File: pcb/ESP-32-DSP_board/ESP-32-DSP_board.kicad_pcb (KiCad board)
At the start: 2 copper layers, 40.4 x 74.6 mm, 56 parts, among them J1 USB_C_Receptacle_USB2.0, J2 Conn_01x04_Pin, J3 Conn_01x04_Pin, J4 Conn_01x07_Pin, J5 Conn_01x07_Pin, Q1 BC847, Q2 BC847, SW1 Reset, SW2 Boot, U1 AZ1117IH-3.3, U2 ESP32-WROOM-32UE-N8, U3 USBLC6-2P6, U4 CP2104, U5 ADS8688

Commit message: Separated GND and GNDA
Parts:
- added NT1: NetTie_2, NetTie:NetTie-2_THT_Pad1.0mm, F.Cu at (104.1, 86.6)
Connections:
- C19 pad 2: Net-(U5-AIN_0GND) -> GNDA
- C20 pad 2: Net-(U5-AIN_1GND) -> GNDA
- C21 pad 1: Net-(U5-AIN_2GND) -> GNDA
- C22 pad 1: Net-(U5-AIN_3GND) -> GNDA
- C23 pad 1: Net-(U5-AIN_4GND) -> GNDA
- C24 pad 1: Net-(U5-AIN_5GND) -> GNDA
- C25 pad 2: Net-(U5-AIN_6GND) -> GNDA
- C26 pad 1: Net-(U5-AIN_7GND) -> GNDA
- U5 pad 10: GND -> GNDA
- U5 pad 11: GND -> GNDA
- U5 pad 13: Net-(U5-AIN_6GND) -> GNDA
- U5 pad 15: Net-(U5-AIN_7GND) -> GNDA
- U5 pad 17: Net-(U5-AIN_0GND) -> GNDA
- U5 pad 19: Net-(U5-AIN_1GND) -> GNDA
- U5 pad 20: Net-(U5-AIN_2GND) -> GNDA
- U5 pad 22: Net-(U5-AIN_3GND) -> GNDA
- U5 pad 24: Net-(U5-AIN_4GND) -> GNDA
- U5 pad 26: Net-(U5-AIN_5GND) -> GNDA
- U5 pad 28: GND -> GNDA
- U5 pad 29: GND -> GNDA
- U5 pad 31: GND -> GNDA
- U5 pad 32: GND -> GNDA
- U5 pad 8: GND -> GNDA
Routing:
- net GNDA: track 0.00 -> 95.9 mm, vias 0 -> 12
- net Net-(U5-AIN_6GND): track 8.24 -> 0.00 mm
- net Net-(U5-AIN_1GND): track 8.12 -> 0.00 mm
- net Net-(U5-AIN_7GND): track 7.86 -> 0.00 mm
- net Net-(U5-AIN_0GND): track 7.62 -> 0.00 mm
- net Net-(U5-AIN_2GND): track 7.22 -> 0.00 mm
- net Net-(U5-AIN_3GND): track 7.15 -> 0.00 mm
- net Net-(U5-AIN_4GND): track 6.78 -> 0.00 mm
- net Net-(U5-AIN_5GND): track 6.65 -> 0.00 mm
- net GND: track 160.5 -> 154.1 mm, vias 42 -> 37
- net /ADC_A5: vias 0 -> 1
- net /ADC_A4: vias 0 -> 1
- net /ADC_A3: vias 0 -> 1
- net /ADC_A2: vias 0 -> 1
- added copper zone on B.Cu, net GNDA
- added copper zone on F.Cu, net GNDA

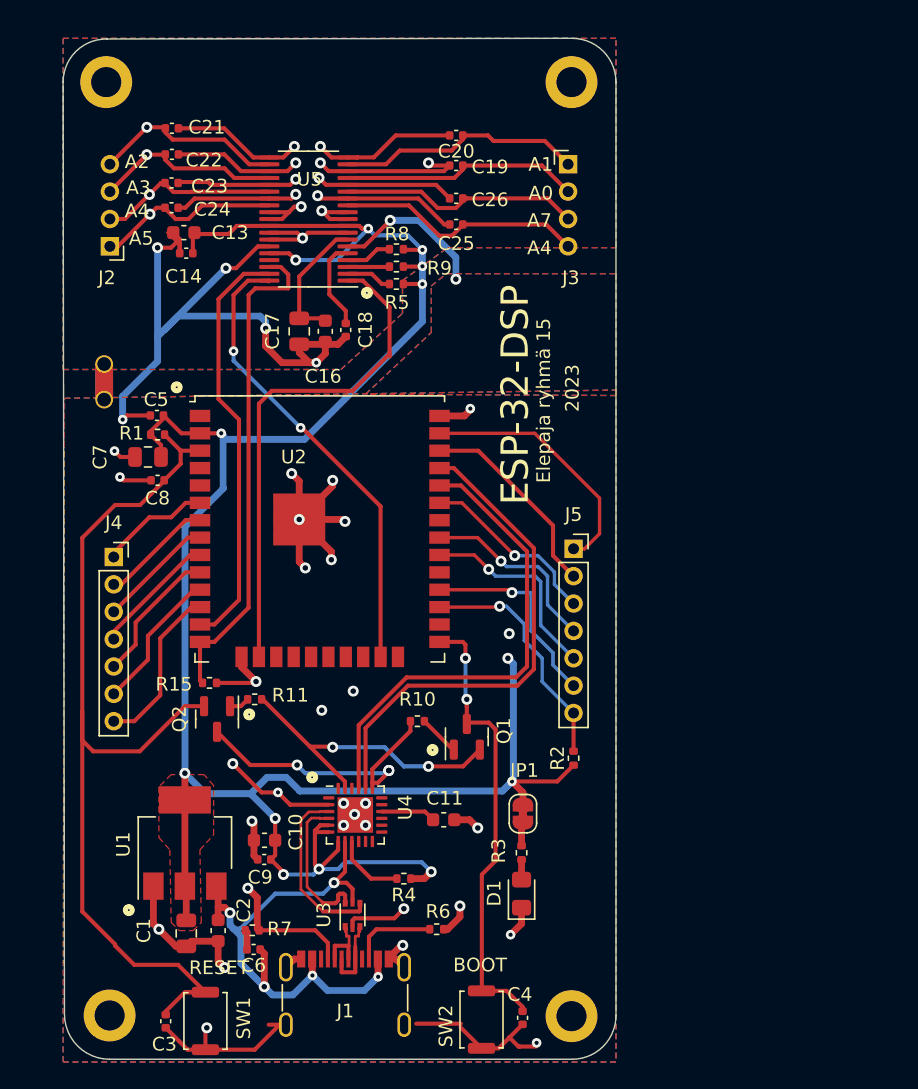
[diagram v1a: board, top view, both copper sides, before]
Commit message: Updated ADC configutation
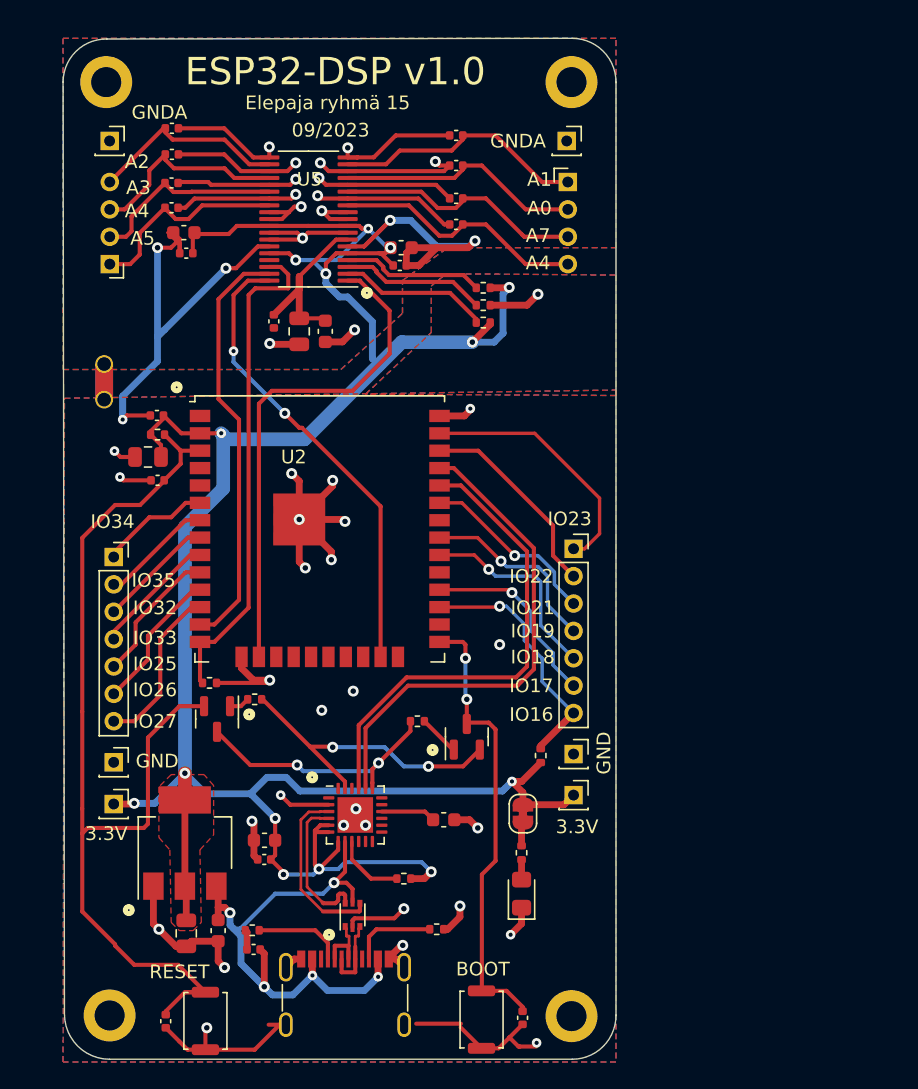
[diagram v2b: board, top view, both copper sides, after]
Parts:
- added C12: 100n, Capacitor_SMD:C_0402_1005Metric, F.Cu at (116.5, 83.5)
- added C15: 100n, Capacitor_SMD:C_0402_1005Metric, F.Cu at (125.7, 79.4)
- added J10: Conn_01x01_Pin, Connector_PinSocket_2.00mm:PinSocket_1x01_P2.00mm_Vertical, F.Cu at (104.5, 70.3)
- added J11: Conn_01x01_Pin, Connector_PinSocket_2.00mm:PinSocket_1x01_P2.00mm_Vertical, F.Cu at (137.9, 70.3)
- added J6: Conn_01x01_Pin, Connector_PinSocket_2.00mm:PinSocket_1x01_P2.00mm_Vertical, F.Cu at (104.8, 115.7)
- added J7: Conn_01x01_Pin, Connector_PinSocket_2.00mm:PinSocket_1x01_P2.00mm_Vertical, F.Cu at (138.4, 115.1)
- added J8: Conn_01x01_Pin, Connector_PinSocket_2.00mm:PinSocket_1x01_P2.00mm_Vertical, F.Cu at (104.8, 118.8)
- added J9: Conn_01x01_Pin, Connector_PinSocket_2.00mm:PinSocket_1x01_P2.00mm_Vertical, F.Cu at (138.4, 118.1)
- C18: value 100n -> 1u; footprint Capacitor_SMD:C_0402_1005Metric -> Capacitor_SMD:C_0603_1608Metric
- C19, C20, C21, C22, C23, C24, C25, C26: value 10n -> 1n
- moved C18 7.24 mm to (125.8, 78.1), turned to 0 degrees
- moved R5 6.94 mm to (131.8, 83.6)
- moved R8 6.94 mm to (131.8, 81.0), turned to 0 degrees
- moved R9 6.94 mm to (131.8, 82.3)
- moved R2 2.41 mm to (136.0, 115.2)
- moved J3 1.30 mm to (138.0, 73.3)
- moved J2 1.30 mm to (104.5, 79.3)
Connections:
- C16 pad 2: GND -> GNDA
- C17 pad 2: GND -> GNDA
- C18 pad 1: /ADC_REF_Voltage -> +3.3V
- C18 pad 2: GND -> GNDA
- R8 pad 1: +3.3V -> Net-(U5-~{REFSEL})
- R8 pad 2: Net-(U5-~{REFSEL}) -> +3.3V
- R9 pad 2: +3.3V -> GND
- U5 pad 5: /ADC_REF_Voltage -> +3.3V
- U5 pad 6: GND -> GNDA
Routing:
- net GND: track 154.1 -> 122.9 mm, vias 37 -> 31
- net GNDA: track 95.9 -> 119.9 mm, vias 12 -> 16
- net +3.3V: track 172.4 -> 187.5 mm, vias 13 -> 14
- net Net-(U5-~{RST/PD}): track 3.36 -> 11.0 mm
- net Net-(U5-DAISY): track 3.06 -> 10.6 mm
- net Net-(U5-~{REFSEL}): track 3.38 -> 10.3 mm
- net /ADC_REF_Voltage: track 6.83 -> 0.00 mm
- net Net-(U5-REFCAP): track 9.98 -> 13.5 mm
- net /EN: track 70.3 -> 73.9 mm
- net Net-(J1-CC1): track 9.87 -> 6.58 mm, vias 1 -> 0
- net /RTS: track 21.3 -> 19.3 mm, vias 3 -> 2
- net /ADC_A5: track 13.6 -> 15.1 mm, vias 1 -> 0
- net /ADC_A4: track 13.0 -> 14.2 mm, vias 1 -> 0
- net /ADC_A3: track 13.7 -> 14.9 mm, vias 1 -> 0
- net /IO17: track 14.9 -> 14.0 mm
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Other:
- board text added: "09/2023"
- board text added: "3.3V"
- board text added: "ESP32-DSP v1.0"
- board text added: "GND"
- board text added: "GNDA"
- board text added: "IO16"
- board text added: "IO17"
- board text added: "IO18"
- board text added: "IO19"
- board text added: "IO21"
- board text added: "IO22"
- board text added: "IO23"
- board text added: "IO25"
- board text added: "IO26"
- board text added: "IO27"
- board text added: "IO32"
- board text added: "IO33"
- board text added: "IO34"
- board text added: "IO35"
- board text removed: "2023"
- board text removed: "ESP-32-DSP"

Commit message: ESP32-S3 version of dsp board with SD-card and DAC added
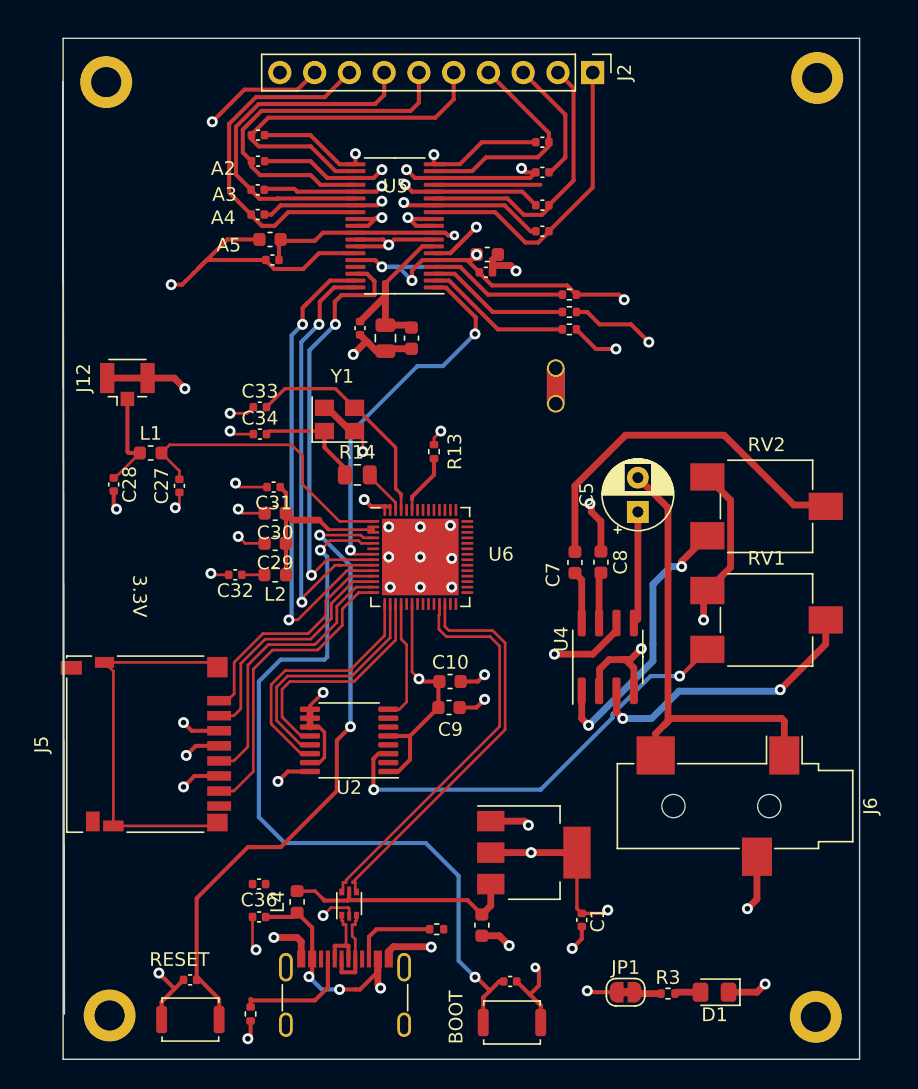
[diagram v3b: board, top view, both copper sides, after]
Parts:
- removed C11: 4.7u, Capacitor_SMD:C_0603_1608Metric
- removed J10, J11, J7, J8, J9: Conn_01x01_Pin, Connector_PinSocket_2.00mm:PinSocket_1x01_P2.00mm_Vertical
- removed J3: Conn_01x04_Pin, Connector_PinHeader_2.00mm:PinHeader_1x04_P2.00mm_Horizontal
- removed J4: Conn_01x07_Pin, Connector_PinSocket_2.00mm:PinSocket_1x07_P2.00mm_Vertical
- removed Q1, Q2: BC847, Package_TO_SOT_SMD:SOT-23
- removed R1, R15, R2: 10k, Resistor_SMD:R_0402_1005Metric
- removed R10, R11, R4: 4.7k, Resistor_SMD:R_0402_1005Metric
- added C27: 3.3p, Capacitor_SMD:C_0402_1005Metric, F.Cu at (109.6, 95.5)
- added C28: 3.3p, Capacitor_SMD:C_0402_1005Metric, F.Cu at (104.8, 95.4)
- added C29: 10u, Capacitor_SMD:C_0603_1608Metric, F.Cu at (116.6, 99.7)
- added C30: 1u, Capacitor_SMD:C_0603_1608Metric, F.Cu at (116.6, 97.5)
- added C31: 100n, Capacitor_SMD:C_0402_1005Metric, F.Cu at (116.5, 95.6)
- added C32: 100n, Capacitor_SMD:C_0402_1005Metric, F.Cu at (113.7, 102.0)
- added C33: 12p, Capacitor_SMD:C_0402_1005Metric, F.Cu at (115.5, 89.8)
- added C34: 12p, Capacitor_SMD:C_0402_1005Metric, F.Cu at (115.5, 91.7)
- added C36: 100n, Capacitor_SMD:C_0402_1005Metric, F.Cu at (115.4, 124.6)
- added J12: Conn_Coaxial, Connector_Coaxial:U.FL_Hirose_U.FL-R-SMT-1_Vertical, F.Cu at (105.8, 88.1)
- added L1: 2.2n, Inductor_SMD:L_0603_1608Metric, F.Cu at (107.5, 93.1)
- added L2: 2.2n, Inductor_SMD:L_0603_1608Metric, F.Cu at (116.6, 102.0)
- added L4: 2.2n, Inductor_SMD:L_0603_1608Metric, F.Cu at (118.2, 125.9)
- added R13: 10k, Resistor_SMD:R_0402_1005Metric, F.Cu at (128.2, 93.0)
- added R14: 10, Resistor_SMD:R_0805_2012Metric, F.Cu at (122.6, 94.7)
- added RV1: R_Potentiometer, Potentiometer_SMD:Potentiometer_ACP_CA6-VSMD_Vertical, F.Cu at (152.5, 105.3)
- added RV2: R_Potentiometer, Potentiometer_SMD:Potentiometer_ACP_CA6-VSMD_Vertical, F.Cu at (152.5, 97.0)
- added U6: ESP32-S3FH4R2, Package_DFN_QFN:QFN-56-1EP_7x7mm_P0.4mm_EP5.6x5.6mm, F.Cu at (127.2, 100.7)
- added Y1: 40MHz, Crystal:Crystal_SMD_3225-4Pin_3.2x2.5mm, F.Cu at (121.3, 90.7)
- C1: footprint Capacitor_SMD:C_0805_2012Metric -> Capacitor_SMD:C_0402_1005Metric
- C10: value 4.7u -> 10u
- C5: value 100n -> 250u; footprint Capacitor_SMD:C_0402_1005Metric -> Capacitor_THT:CP_Radial_D5.0mm_P2.50mm
- C7: value 22u -> 10u; footprint Capacitor_SMD:C_0805_2012Metric -> Capacitor_SMD:C_0603_1608Metric
- C8: value 1u -> 10u; footprint Capacitor_SMD:C_0402_1005Metric -> Capacitor_SMD:C_0603_1608Metric
- C9: footprint Capacitor_SMD:C_0402_1005Metric -> Capacitor_SMD:C_0603_1608Metric
- J2: value Conn_01x04_Pin -> Conn_01x10_Pin; footprint Connector_PinHeader_2.00mm:PinHeader_1x04_P2.00mm_Horizontal -> Connector_PinHeader_2.54mm:PinHeader_1x10_P2.54mm_Vertical
- J5: value Conn_01x07_Pin -> SD_Card; footprint Connector_PinSocket_2.00mm:PinSocket_1x07_P2.00mm_Vertical -> Connector_Card:microSD_HC_Hirose_DM3D-SF
- J6: value Conn_01x01_Pin -> AudioJack2_Ground; footprint Connector_PinSocket_2.00mm:PinSocket_1x01_P2.00mm_Vertical -> Connector_Audio:Jack_3.5mm_CUI_SJ-3523-SMT_Horizontal
- U2: value ESP32-WROOM-32UE-N8 -> AD5689BRUZ; footprint RF_Module:ESP32-WROOM-32U -> Package_SO:TSSOP-16_4.4x5mm_P0.65mm
- U4: value CP2104 -> LM386; footprint Package_DFN_QFN:QFN-24-1EP_4x4mm_P0.5mm_EP2.6x2.6mm -> Package_SO:SOIC-8_3.9x4.9mm_P1.27mm
- moved J6 45.5 mm to (150.2, 118.9), turned to -90 degrees
- moved J2 38.0 mm to (139.8, 65.3), turned to -90 degrees
- moved C5 35.8 mm to (143.1, 97.4), turned to 90 degrees
- moved J5 34.4 mm to (107.2, 114.4), turned to 90 degrees
- moved NT1 33.0 mm to (137.1, 86.9)
- moved C8 32.9 mm to (140.4, 101.1), turned to -90 degrees
- moved C7 32.1 mm to (138.5, 101.1), turned to 90 degrees
- moved C1 28.9 mm to (139.0, 127.2)
- moved U1 25.5 mm to (135.5, 122.3), turned to 0 degrees
- moved U4 21.8 mm to (140.9, 108.0), turned to 90 degrees
- moved C2 19.3 mm to (131.7, 127.6)
- moved H1 18.0 mm to (156.2, 65.7)
- moved H4 17.9 mm to (156.1, 134.3)
- moved C10 17.8 mm to (129.4, 109.8), turned to 0 degrees
- moved C9 17.5 mm to (129.3, 111.7), turned to 0 degrees
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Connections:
- C2 pad 1: /VBUS -> Net-(U1-VI)
- C5 pad 1: +3.3V -> Net-(C5-Pad1)
- C5 pad 2: GND -> Net-(C5-Pad2)
- C6 pad 1: /VBUS -> +5V
- C7 pad 1: +3.3V -> Net-(C7-Pad1)
- C7 pad 2: GND -> Net-(C7-Pad2)
- C8 pad 1: /EN -> GNDA
- C8 pad 2: GND -> Net-(U4-BYPASS)
- J1 pad A4: /VBUS -> +5V
- J1 pad A9: /VBUS -> +5V
- J1 pad B4: /VBUS -> +5V
- J1 pad B9: /VBUS -> +5V
- J1 pad S1: GND -> unconnected-(J1-SHIELD-PadS1)
- J2 pad 1: /ADC_A5 -> /ADC_A6
- J2 pad 2: /ADC_A4 -> /ADC_A7
- J2 pad 3: /ADC_A3 -> /ADC_A0
- J2 pad 4: /ADC_A2 -> /ADC_A1
- J5 pad 1: /IO23 -> /SD_CS
- J5 pad 2: /IO22 -> /SD_MOSI
- J5 pad 3: /IO21 -> GND
- J5 pad 4: /IO19 -> +3.3V
- J5 pad 5: /IO18 -> /SD_SCLK
- J5 pad 6: /IO17 -> GND
- J5 pad 7: /IO16 -> /SD_MISO
- U1 pad 3: /VBUS -> Net-(U1-VI)
- U2 pad 1: GND -> +3.3V
- U2 pad 10: /IO25 -> +3.3V
- U2 pad 11: /IO26 -> +3.3V
- U2 pad 12: /IO27 -> /DAC_SCLK
- U2 pad 13: /ADC_SCLK -> /DAC_SYNC
- U2 pad 14: /ADC_MISO -> /DAC_MISO
- U2 pad 15: GND -> +3.3V
- U2 pad 16: /ADC_MOSI -> GND
- U2 pad 2: +3.3V -> unconnected-(U2-NC-Pad2)
- U2 pad 3: /EN -> Net-(U2-VOUTA)
- U2 pad 4: unconnected-(U2-SENSOR_VP-Pad4) -> GND
- U2 pad 5: unconnected-(U2-SENSOR_VN-Pad5) -> +3.3V
- U2 pad 6: /IO34 -> unconnected-(U2-NC-Pad6)
- U2 pad 7: /IO35 -> unconnected-(U2-VOUTB-Pad7)
- U2 pad 8: /IO32 -> /DAC_MOSI
- U2 pad 9: /IO33 -> +3.3V
- U3 pad 5: /VBUS -> Net-(U1-VI)
- U4 pad 1: unconnected-(U4-~{RI}-Pad1) -> Net-(RV2-Pad1)
- U4 pad 2: GND -> GNDA
- U4 pad 3: /USB_D+ -> Net-(U4-+)
- U4 pad 4: /USB_D- -> GNDA
- U4 pad 5: +3.3V -> Net-(C5-Pad1)
- U4 pad 6: +3.3V -> +5V
- U4 pad 7: +3.3V -> Net-(U4-BYPASS)
- U4 pad 8: /VBUS -> Net-(C7-Pad1)
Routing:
- net +5V: track 0.00 -> 135.2 mm, vias 0 -> 4
- net +3.3V: track 187.5 -> 107.2 mm
- net GNDA: track 119.9 -> 176.5 mm, vias 16 -> 19
- net /VBUS: track 40.0 -> 0.00 mm, vias 5 -> 0
- net /TX: track 36.7 -> 0.00 mm
- net /RX: track 35.5 -> 0.00 mm
- net Net-(C5-Pad2): track 0.00 -> 33.1 mm
- net Net-(U2-VOUTA): track 0.00 -> 32.3 mm, vias 0 -> 2
- net unconnected-(J5-WRITE_PROTECT-Pad11): track 0.00 -> 28.3 mm
- net Net-(C7-Pad2): track 0.00 -> 26.8 mm
- net /EN: track 73.9 -> 47.2 mm, vias 0 -> 2
- net /IO0: track 33.1 -> 57.5 mm
- net GND: track 122.9 -> 99.0 mm, vias 31 -> 37
- net /DTR: track 22.5 -> 0.00 mm, vias 2 -> 0
- net /SD_MISO: track 0.00 -> 22.4 mm
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- added copper zone on In2.Cu, net +3.3V
- added copper zone on In1.Cu, net GND
- added copper zone on In1.Cu, net GNDA
- removed copper zone on F.Cu, net +3.3V
- removed copper zone on B.Cu, net GND
- removed copper zone on F.Cu, net GND
- removed copper zone on B.Cu, net GNDA
- removed copper zone on F.Cu, net GNDA
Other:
- board size 40.4 x 74.6 mm -> 58.2 x 74.6 mm
- copper layers 2 -> 4
- board text removed: "09/2023"
- board text removed: "A0"
- board text removed: "A1"
- board text removed: "A7"
- board text removed: "ESP32-DSP v1.0"
- board text removed: "Elepaja ryhmä 15"
- board text removed: "GND"
- board text removed: "GNDA"
- board text removed: "IO16"
- board text removed: "IO17"
- board text removed: "IO18"
- board text removed: "IO19"
- board text removed: "IO21"
- board text removed: "IO22"
- board text removed: "IO23"
- board text removed: "IO25"
- board text removed: "IO26"
- board text removed: "IO27"
- board text removed: "IO32"
- board text removed: "IO33"
- board text removed: "IO34"
- board text removed: "IO35"

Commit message: First working version of S3 dsp board
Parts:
- added J3: AudioJack2_Ground, Connector_Audio:Jack_3.5mm_CUI_SJ-3523-SMT_Horizontal, F.Cu at (150.3, 123.6)
- added J4: Conn_01x08_Pin, Connector_PinHeader_2.54mm:PinHeader_1x08_P2.54mm_Vertical, F.Cu at (153.1, 71.1)
- added J7: Conn_01x08_Pin, Connector_PinHeader_2.54mm:PinHeader_1x08_P2.54mm_Vertical, F.Cu at (149.1, 71.1)
- J6: value AudioJack2_Ground -> Conn_01x08_Pin; footprint Connector_Audio:Jack_3.5mm_CUI_SJ-3523-SMT_Horizontal -> Connector_PinHeader_2.54mm:PinHeader_1x08_P2.54mm_Vertical
- moved J6 48.3 mm to (157.1, 71.1), turned to 0 degrees
- moved C5 16.3 mm to (147.4, 113.1), turned to -90 degrees
- moved C16 14.2 mm to (134.8, 73.1), turned to 0 degrees
- moved C17 14.0 mm to (134.8, 75.0), turned to 0 degrees
- moved C12 13.3 mm to (134.1, 76.9), turned to 180 degrees
- moved C10 13.0 mm to (121.9, 120.4), turned to -90 degrees
- moved C9 12.8 mm to (120.0, 120.4), turned to -90 degrees
- moved C33 9.98 mm to (125.2, 92.0), turned to -90 degrees
- moved R5 6.14 mm to (132.1, 85.4)
- moved R8 6.14 mm to (132.1, 82.8)
- moved R9 6.14 mm to (132.1, 84.1)
- moved C20 5.68 mm to (130.5, 71.2)
- moved C25 5.63 mm to (130.6, 75.8)
- moved R14 5.56 mm to (118.0, 91.5), turned to 90 degrees
- moved C26 5.55 mm to (130.6, 74.4)
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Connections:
- net Net-(U5-REFCAP) renamed /ADC_REF_CAP
- J5 pad 10: unconnected-(J5-CARD_DETECT-Pad10) -> GND
- J5 pad 11: unconnected-(J5-WRITE_PROTECT-Pad11) -> GND
- U6 pad 29: unconnected-(U6-VDD_SPI-Pad29) -> +3.3V
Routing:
- net /IO17: track 0.00 -> 53.5 mm, vias 0 -> 1
- net /IO16: track 0.00 -> 51.4 mm, vias 0 -> 1
- net /IO15: track 0.00 -> 51.0 mm, vias 0 -> 1
- net /IO18: track 0.00 -> 49.9 mm, vias 0 -> 1
- net /IO14: track 0.00 -> 49.7 mm, vias 0 -> 1
- net +5V: track 135.2 -> 183.9 mm
- net /IO21: track 0.00 -> 45.8 mm
- net /IO46: track 0.00 -> 36.5 mm
- net /IO48: track 0.00 -> 36.3 mm
- net /IO47: track 0.00 -> 32.9 mm
- net /IO42: track 0.00 -> 31.5 mm
- net /IO41: track 0.00 -> 28.9 mm
- net +3.3V: track 107.2 -> 136.1 mm, vias 14 -> 17
- net unconnected-(J5-WRITE_PROTECT-Pad11): track 28.3 -> 0.00 mm
- net /IO38: track 0.00 -> 27.3 mm
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- added copper zone on F.Cu, net +3.3V
- added copper zone on F.Cu, net GNDA
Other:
- outline, holes or cut-outs redrawn
- board text added: "J6"
- board text removed: "3.3V"
- board text removed: "A3"
- board text removed: "A5"
